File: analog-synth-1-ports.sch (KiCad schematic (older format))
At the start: 12 parts

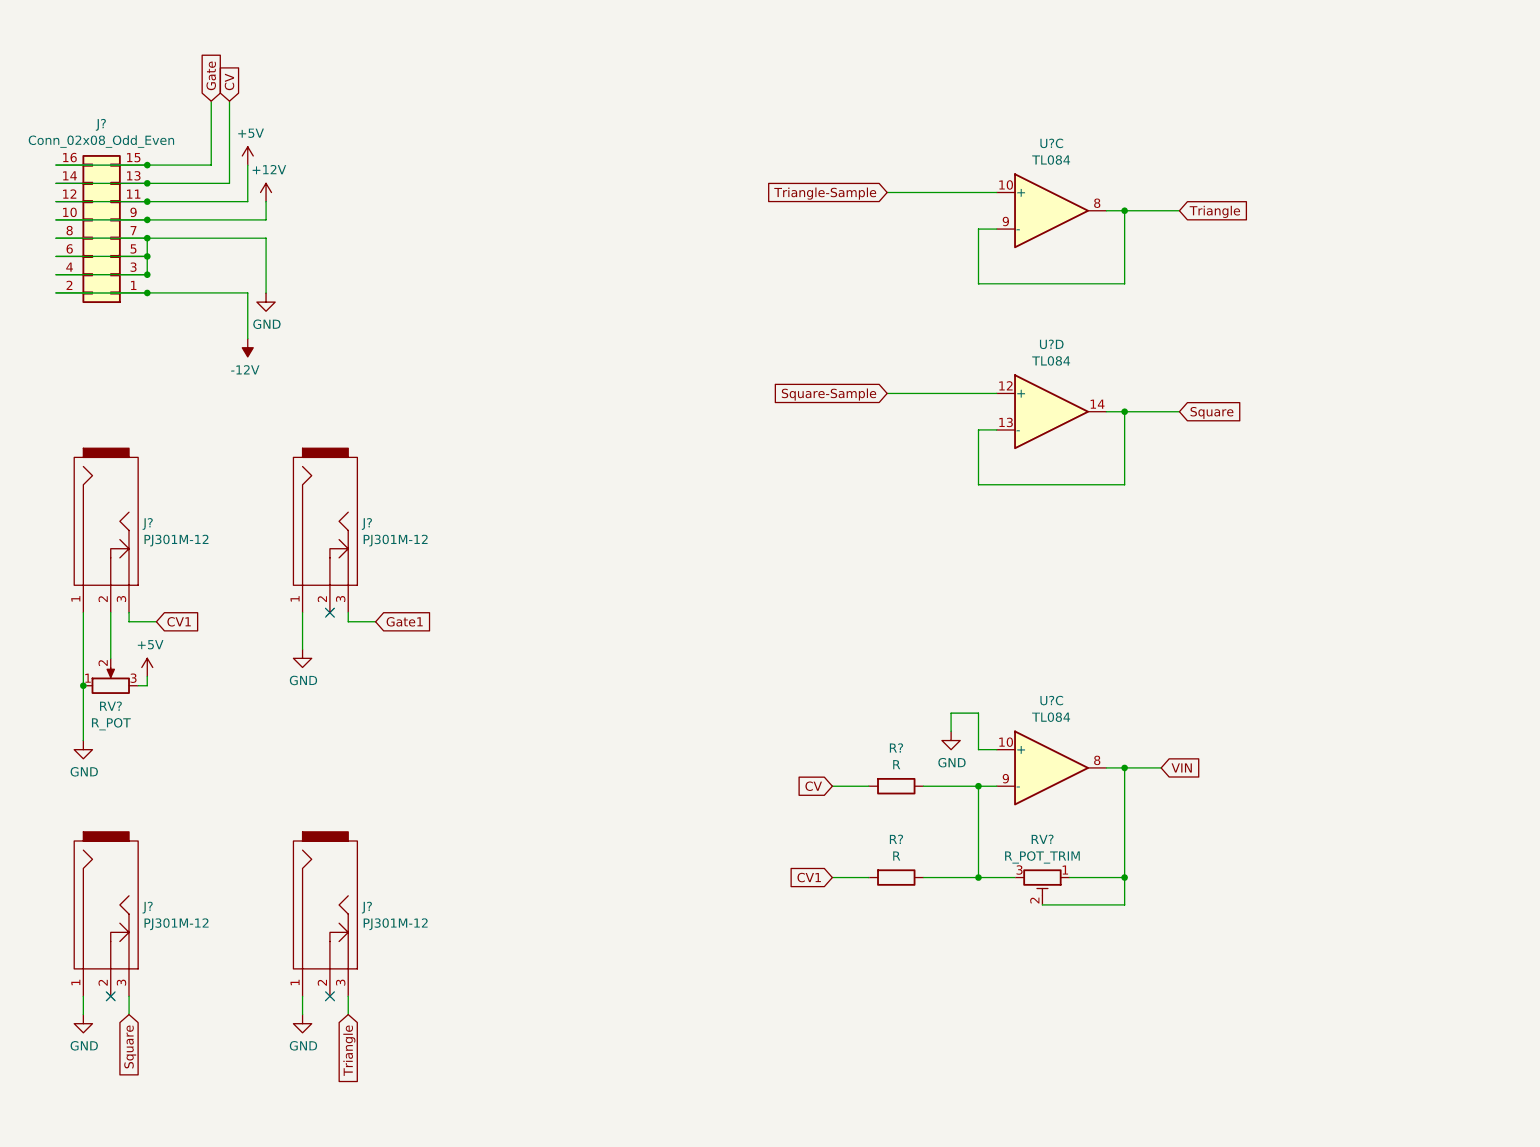
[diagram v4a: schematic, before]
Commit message: Finish basic synth circuit diagram
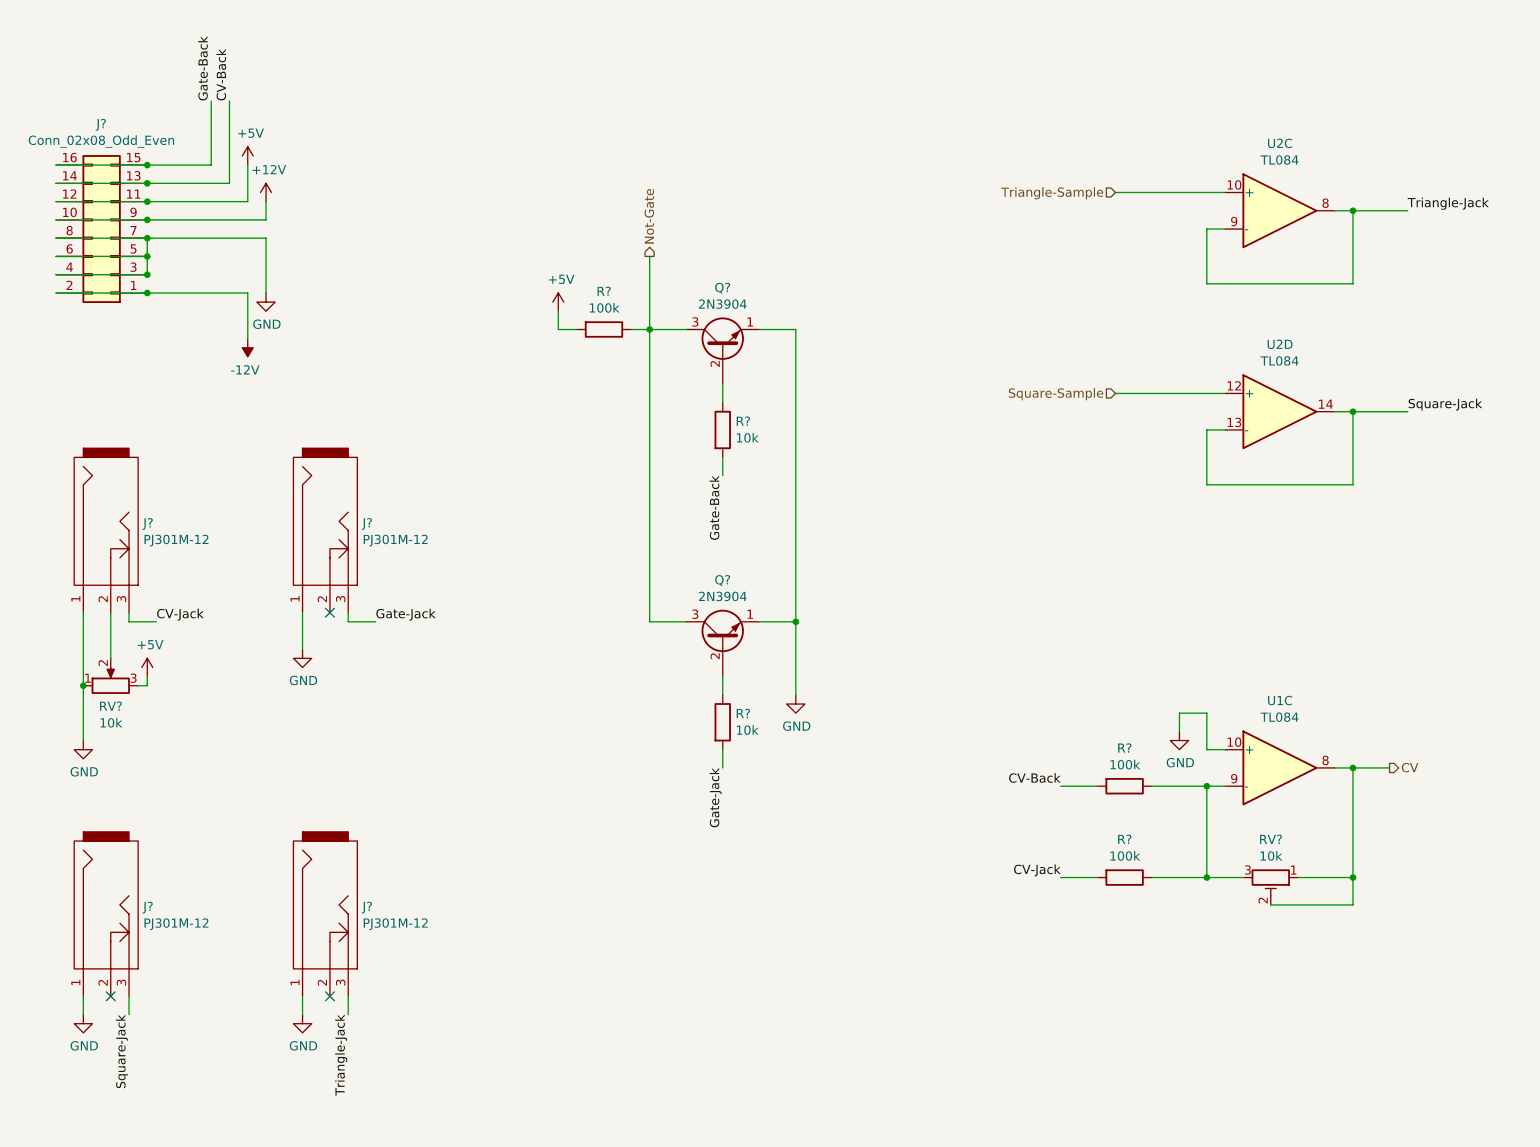
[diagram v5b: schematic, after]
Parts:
- added Q? (x2): 2N3904, Package_TO_SOT_THT:TO-92_Inline, symbol Transistor_BJT:2N3904
- added R? (x2): 10k, symbol Device:R
- added R?: 100k, symbol Device:R
- R? (x2): value R -> 100k
- RV?: value R_POT -> 10k
- RV?: value R_POT_TRIM -> 10k
- gave numbers to parts that had none: 2
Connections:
- net VIN is gone; now on net CV: RV?.1, RV?.2, U1.8
- net +5V: now also R?.2
- net CV: no longer J?.13 (Pin_13), J?.14 (Pin_14), R?.2
- net GND: now also Q?.1 (E), Q?.1 (E)
- net CV1 renamed CV-Jack
- net Gate renamed Gate-Back
- net Gate-Back: now also R?.2
- net Gate1 renamed Gate-Jack
- net Gate-Jack: now also R?.2
- net Square renamed Square-Jack
- net Triangle renamed Triangle-Jack
- new net: Q?.2 (B), R?.1 (x2)
- new net CV-Back: J?.13 (Pin_13), J?.14 (Pin_14), R?.2
- new net Not-Gate: Q?.3 (C), Q?.3 (C), R?.1
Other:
- moved on the sheet: R?, RV?, U1C, U2C, U2D

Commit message: Annotate components
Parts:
- gave numbers to parts that had none: 14
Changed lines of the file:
@@
 $EndDescr
 $Comp
-L Connector_Generic:Conn_02x08_Odd_Even J?
+L Connector_Generic:Conn_02x08_Odd_Even J1
 U 1 1 5C85B2BB
 P 2050 2100
-F 0 "J?" H 2100 1475 50  0000 C CNN
+F 0 "J1" H 2100 1475 50  0000 C CNN
 F 1 "Conn_02x08_Odd_Even" H 2100 1566 50  0000 C CNN
 F 2 "" H 2050 2100 50  0001 C CNN
@@
 Connection ~ 2250 2300
 $Comp
-L custom-components:PJ301M-12 J?
+L custom-components:PJ301M-12 J2
 U 1 1 5C87239F
 P 2050 3700
-F 0 "J?" V 2010 3522 50  0000 R CNN
+F 0 "J2" V 2010 3522 50  0000 R CNN
 F 1 "PJ301M-12" V 2101 3522 50  0000 R CNN
 F 2 "" H 2050 3700 50  0000 C CNN
@@
 $EndComp
 $Comp
-L custom-components:PJ301M-12 J?
+L custom-components:PJ301M-12 J4
 U 1 1 5C87271A
 P 3250 3700
-F 0 "J?" V 3210 3522 50  0000 R CNN
+F 0 "J4" V 3210 3522 50  0000 R CNN
 F 1 "PJ301M-12" V 3301 3522 50  0000 R CNN
 F 2 "" H 3250 3700 50  0000 C CNN
@@
 $EndComp
 $Comp
-L custom-components:PJ301M-12 J?
+L custom-components:PJ301M-12 J3
 U 1 1 5C8727CB
 P 2050 5800
-F 0 "J?" V 2010 5622 50  0000 R CNN
+F 0 "J3" V 2010 5622 50  0000 R CNN
 F 1 "PJ301M-12" V 2101 5622 50  0000 R CNN
 F 2 "" H 2050 5800 50  0000 C CNN
@@
 $EndComp
 $Comp
-L custom-components:PJ301M-12 J?
+L custom-components:PJ301M-12 J5
 U 1 1 5C872841
 P 3250 5800
-F 0 "J?" V 3210 5622 50  0000 R CNN
+F 0 "J5" V 3210 5622 50  0000 R CNN
 F 1 "PJ301M-12" V 3301 5622 50  0000 R CNN
 F 2 "" H 3250 5800 50  0000 C CNN
@@
 NoConn ~ 2050 6250
 $Comp
-L power:GND #PWR?
+L power:GND #PWR018
 U 1 1 5C877B99
 P 3100 6350
-F 0 "#PWR?" H 3100 6100 50  0001 C CNN
+F 0 "#PWR018" H 3100 6100 50  0001 C CNN
 F 1 "GND" H 3105 6177 50  0000 C CNN
 F 2 "" H 3100 6350 50  0001 C CNN
@@
 $EndComp
 $Comp
-L Device:R_POT_TRIM RV?
+L Device:R_POT_TRIM RV2
 U 1 1 5C87DFED
 P 8400 5600
-F 0 "RV?" V 8193 5600 50  0000 C CNN
+F 0 "RV2" V 8193 5600 50  0000 C CNN
 F 1 "10k" V 8284 5600 50  0000 C CNN
 F 2 "" H 8400 5600 50  0001 C CNN
@@
 Connection ~ 8850 5600
 $Comp
-L power:GND #PWR?
+L power:GND #PWR021
 U 1 1 5C880099
 P 7900 4800
-F 0 "#PWR?" H 7900 4550 50  0001 C CNN
+F 0 "#PWR021" H 7900 4550 50  0001 C CNN
 F 1 "GND" H 7905 4627 50  0000 C CNN
 F 2 "" H 7900 4800 50  0001 C CNN
@@
 	7900 4700 7900 4800
 $Comp
-L Device:R R?
+L Device:R R4
 U 1 1 5C880E42
 P 7600 5100
-F 0 "R?" V 7393 5100 50  0000 C CNN
+F 0 "R4" V 7393 5100 50  0000 C CNN
 F 1 "100k" V 7484 5100 50  0000 C CNN
 F 2 "" V 7530 5100 50  0001 C CNN
@@
 $EndComp
 $Comp
-L Device:R R?
+L Device:R R5
 U 1 1 5C880EB3
 P 7600 5600
-F 0 "R?" V 7393 5600 50  0000 C CNN
+F 0 "R5" V 7393 5600 50  0000 C CNN
 F 1 "100k" V 7484 5600 50  0000 C CNN
 F 2 "" V 7530 5600 50  0001 C CNN
@@
 Connection ~ 1900 4550
 $Comp
-L Device:R_POT RV?
+L Device:R_POT RV1
 U 1 1 5C872CCA
 P 2050 4550
-F 0 "RV?" V 1936 4550 50  0000 C CNN
+F 0 "RV1" V 1936 4550 50  0000 C CNN
 F 1 "10k" V 1845 4550 50  0000 C CNN
 F 2 "" H 2050 4550 50  0001 C CNN
@@
 $EndComp
 $Comp
-L power:GND #PWR?
+L power:GND #PWR011
 U 1 1 5C876B03
 P 1900 6350
-F 0 "#PWR?" H 1900 6100 50  0001 C CNN
+F 0 "#PWR011" H 1900 6100 50  0001 C CNN
 F 1 "GND" H 1905 6177 50  0000 C CNN
 F 2 "" H 1900 6350 50  0001 C CNN
@@
 $EndComp
 $Comp
-L power:GND #PWR?
+L power:GND #PWR017
 U 1 1 5C875167
 P 3100 4350
-F 0 "#PWR?" H 3100 4100 50  0001 C CNN
+F 0 "#PWR017" H 3100 4100 50  0001 C CNN
 F 1 "GND" H 3105 4177 50  0000 C CNN
 F 2 "" H 3100 4350 50  0001 C CNN
@@
 $EndComp
 $Comp
-L power:GND #PWR?
+L power:GND #PWR010
 U 1 1 5C873F44
 P 1900 4850
-F 0 "#PWR?" H 1900 4600 50  0001 C CNN
+F 0 "#PWR010" H 1900 4600 50  0001 C CNN
 F 1 "GND" H 1905 4677 50  0000 C CNN
 F 2 "" H 1900 4850 50  0001 C CNN
@@
 $EndComp
 $Comp
-L power:+5V #PWR?
+L power:+5V #PWR012
 U 1 1 5C87478A
 P 2250 4500
-F 0 "#PWR?" H 2250 4350 50  0001 C CNN
+F 0 "#PWR012" H 2250 4350 50  0001 C CNN
 F 1 "+5V" H 2265 4673 50  0000 C CNN
 F 2 "" H 2250 4500 50  0001 C CNN
@@
 	2600 1350 2600 1700
 $Comp
-L power:-12V #PWR?
+L power:-12V #PWR014
 U 1 1 5C85BF08
 P 2800 2650
-F 0 "#PWR?" H 2800 2750 50  0001 C CNN
+F 0 "#PWR014" H 2800 2750 50  0001 C CNN
 F 1 "-12V" H 2815 2823 50  0000 C CNN
 F 2 "" H 2800 2650 50  0001 C CNN
@@
 $EndComp
 $Comp
-L power:GND #PWR?
+L power:GND #PWR016
 U 1 1 5C85BD09
 P 2900 2400
-F 0 "#PWR?" H 2900 2150 50  0001 C CNN
+F 0 "#PWR016" H 2900 2150 50  0001 C CNN
 F 1 "GND" H 2905 2227 50  0000 C CNN
 F 2 "" H 2900 2400 50  0001 C CNN
@@
 $EndComp
 $Comp
-L power:+12V #PWR?
+L power:+12V #PWR015
 U 1 1 5C85B8F4
 P 2900 1900
-F 0 "#PWR?" H 2900 1750 50  0001 C CNN
+F 0 "#PWR015" H 2900 1750 50  0001 C CNN
 F 1 "+12V" H 2915 2073 50  0000 C CNN
 F 2 "" H 2900 1900 50  0001 C CNN
@@
 $EndComp
 $Comp
-L power:+5V #PWR?
+L power:+5V #PWR013
 U 1 1 5C85B77F
 P 2800 1700
-F 0 "#PWR?" H 2800 1550 50  0001 C CNN
+F 0 "#PWR013" H 2800 1550 50  0001 C CNN
 F 1 "+5V" H 2815 1873 50  0000 C CNN
 F 2 "" H 2800 1700 50  0001 C CNN
@@
 Square-Jack
 $Comp
-L Transistor_BJT:2N3904 Q?
+L Transistor_BJT:2N3904 Q2
 U 1 1 5C88672F
 P 5400 4300
-F 0 "Q?" V 5728 4300 50  0000 C CNN
+F 0 "Q2" V 5728 4300 50  0000 C CNN
 F 1 "2N3904" V 5637 4300 50  0000 C CNN
 F 2 "Package_TO_SOT_THT:TO-92_Inline" H 5600 4225 50  0001 L CIN
@@
 $EndComp
 $Comp
-L Transistor_BJT:2N3904 Q?
+L Transistor_BJT:2N3904 Q1
 U 1 1 5C8869D4
 P 5400 2700
-F 0 "Q?" V 5728 2700 50  0000 C CNN
+F 0 "Q1" V 5728 2700 50  0000 C CNN
 F 1 "2N3904" V 5637 2700 50  0000 C CNN
 F 2 "Package_TO_SOT_THT:TO-92_Inline" H 5600 2625 50  0001 L CIN
@@
 $EndComp
 $Comp
-L Device:R R?
+L Device:R R2
 U 1 1 5C888524
 P 5400 3150
-F 0 "R?" H 5470 3196 50  0000 L CNN
+F 0 "R2" H 5470 3196 50  0000 L CNN
 F 1 "10k" H 5470 3105 50  0000 L CNN
 F 2 "" V 5330 3150 50  0001 C CNN
@@
 $EndComp
 $Comp
-L Device:R R?
+L Device:R R3
 U 1 1 5C888587
 P 5400 4750
-F 0 "R?" H 5470 4796 50  0000 L CNN
+F 0 "R3" H 5470 4796 50  0000 L CNN
 F 1 "10k" H 5470 4705 50  0000 L CNN
 F 2 "" V 5330 4750 50  0001 C CNN
@@
 	5400 4900 5400 5000
 $Comp
-L power:GND #PWR?
+L power:GND #PWR020
 U 1 1 5C88EC7D
 P 5800 4600
-F 0 "#PWR?" H 5800 4350 50  0001 C CNN
+F 0 "#PWR020" H 5800 4350 50  0001 C CNN
 F 1 "GND" H 5805 4427 50  0000 C CNN
 F 2 "" H 5800 4600 50  0001 C CNN
@@
 Connection ~ 5000 2600
 $Comp
-L Device:R R?
+L Device:R R1
 U 1 1 5C894D95
 P 4750 2600
-F 0 "R?" V 4543 2600 50  0000 C CNN
+F 0 "R1" V 4543 2600 50  0000 C CNN
 F 1 "100k" V 4634 2600 50  0000 C CNN
 F 2 "" V 4680 2600 50  0001 C CNN
@@
 $EndComp
 $Comp
-L power:+5V #PWR?
+L power:+5V #PWR019
 U 1 1 5C894E75
 P 4500 2500
-F 0 "#PWR?" H 4500 2350 50  0001 C CNN
+F 0 "#PWR019" H 4500 2350 50  0001 C CNN
 F 1 "+5V" H 4515 2673 50  0000 C CNN
 F 2 "" H 4500 2500 50  0001 C CNN
